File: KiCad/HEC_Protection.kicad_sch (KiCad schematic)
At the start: 32 parts, among them U11 74LS00, U11 74LS32, U12 74LS04, U16 74LS32, U17 74LS74, U18 74LS138, U18 74LS74, U19 74LS30, U22 74LS02, U23 74LS74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

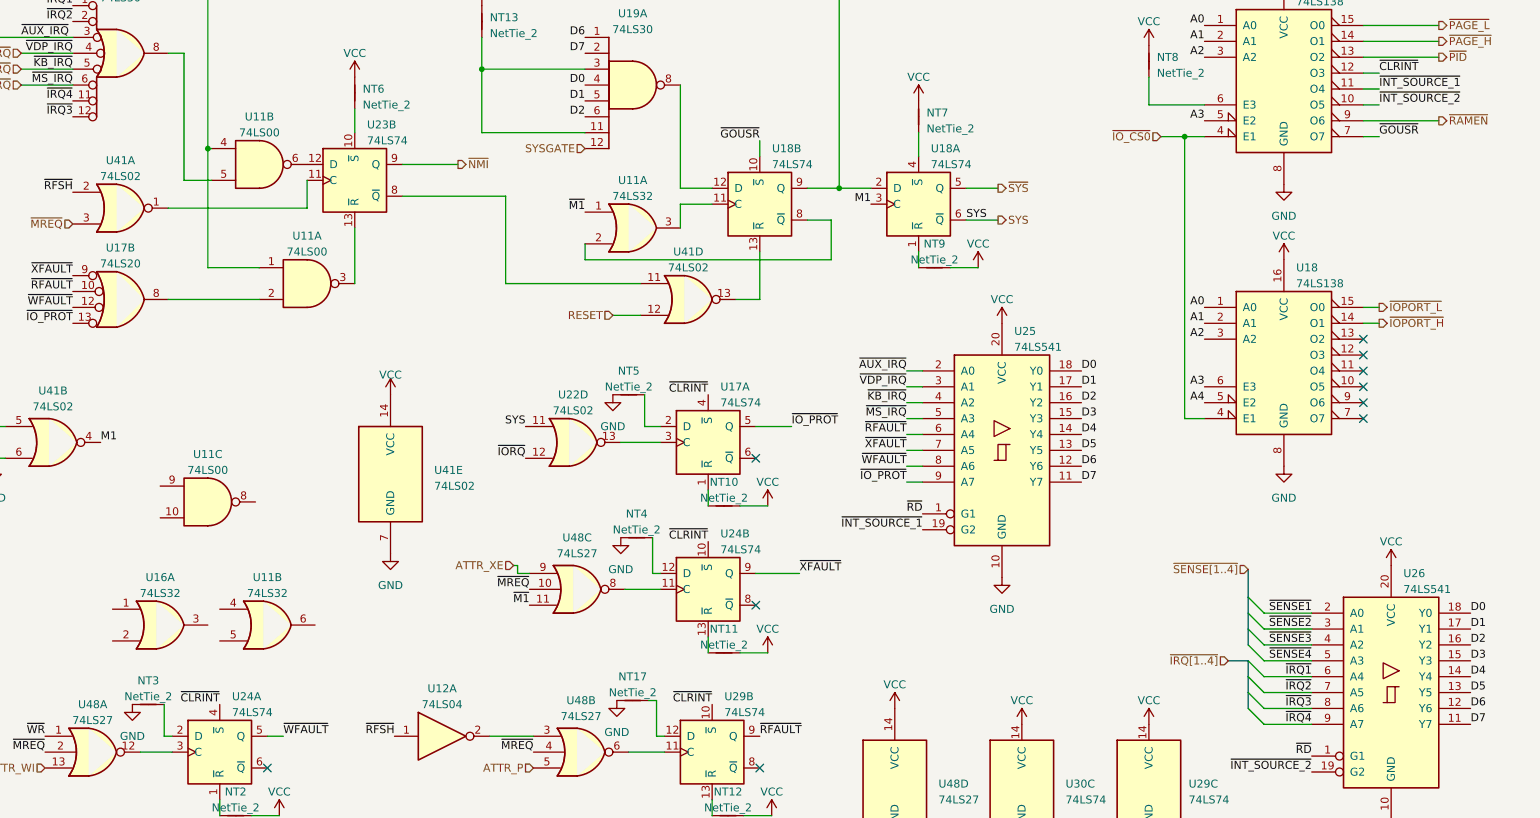
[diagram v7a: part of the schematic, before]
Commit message: Add flash circuit
Changed EEPROM to NOR flash to increase speed. Added circuit to update firmware without requiring a programmer.
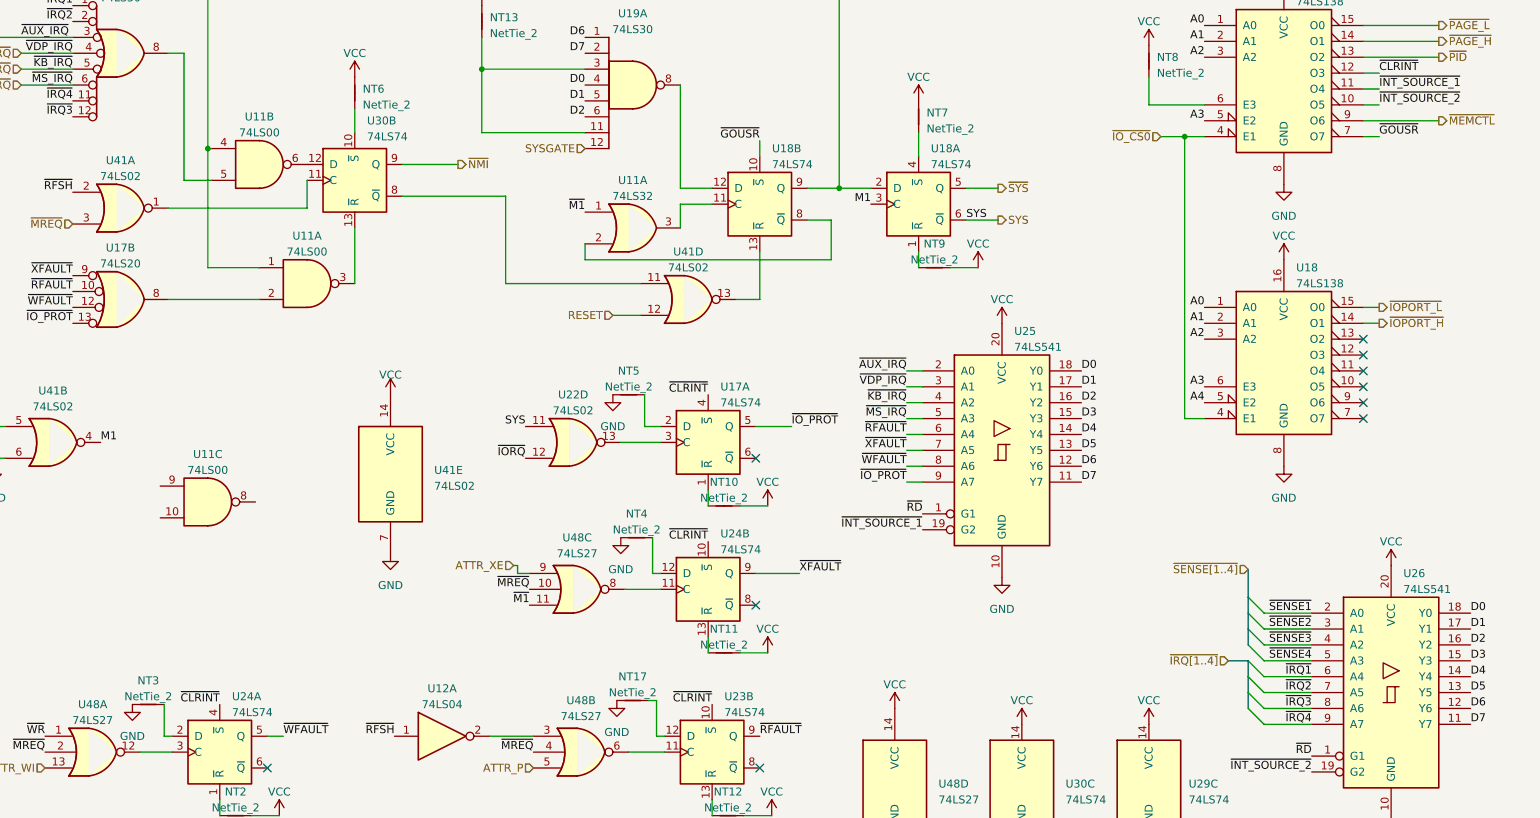
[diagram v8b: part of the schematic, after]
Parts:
- removed U11, U16: 74LS32, Library:DIP-14_W7.62mm_Socket_ThinPads, symbol 74xx:74LS32
- removed unit 2 of U29
- added unit 2 of U30
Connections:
- net ~{CLRINT}: now also U23.10 (~{S})
- net ~{NMI}: now also U30.9 (Q); no longer U23.9 (Q)
- net ~{RFAULT}: now also U23.9 (Q)
- net at U48.6: now also U23.11 (C)
- net at NT17.2: now also U23.12 (D)
- net at NT12.1: now also U23.13 (~{R})
- net at U41.11: now also U30.8 (~{Q}); no longer U23.8 (~{Q})
- net at NT6.1: now also U30.10 (~{S}); no longer U23.10 (~{S})
- net at U41.1: now also U30.11 (C); no longer U23.11 (C)
- net at U11.6: now also U30.12 (D); no longer U23.12 (D)
- net at U11.3: now also U30.13 (~{R}); no longer U23.13 (~{R})
- net ~{RAMEN} renamed ~{MEMCTL}
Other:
- moved on the sheet: U23B
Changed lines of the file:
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@@
     (effects (font (size 1.27 1.27)) (justify right))
   )
-  (hierarchical_label "~{RAMEN}" (shape output) (at 274.955 42.545 0) (fields_autoplaced)
+  (hierarchical_label "~{MEMCTL}" (shape output) (at 274.955 42.545 0) (fields_autoplaced)
     (effects (font (size 1.27 1.27)) (justify left))
   )
@@
     )
   )
-  (symbol (lib_id "74xx:74LS32") (at 87.63 123.19 0) (unit 2)
-    (in_bom yes) (on_board yes) (dnp no) (fields_autoplaced)
-    (property "Reference" "U11" (at 87.63 115.57 0)
-      (effects (font (size 1.27 1.27)))
-    )
-    (property "Value" "74LS32" (at 87.63 118.11 0)
-      (effects (font (size 1.27 1.27)))
-    )
-    (property "Footprint" "Library:DIP-14_W7.62mm_Socket_ThinPads" (at 87.63 123.19 0)
-      (effects (font (size 1.27 1.27)) hide)
-    )
-    (property "Datasheet" "http://www.ti.com/lit/gpn/sn74LS32" (at 87.63 123.19 0)
-      (effects (font (size 1.27 1.27)) hide)
-    )
-    (pin "1")
-    (pin "2")
-    (pin "3")
-    (pin "4")
-    (pin "5")
-    (pin "6")
-    (pin "10")
-    (pin "8")
-    (pin "9")
-    (pin "11")
-    (pin "12")
-    (pin "13")
-    (pin "14")
-    (pin "7")
-    (instances
-      (project "HEC1"
-        (path "/87935374-b60a-4f41-99da-94b76103dd77/73a0c68b-1e42-4c0d-ae31-b1a96d0648bb"
-          (reference "U11") (unit 2)
-        )
-        (path "/87935374-b60a-4f41-99da-94b76103dd77/2930b625-d6a3-4a7f-9d41-a454efcef99d"
-          (reference "U10") (unit 2)
-        )
-      )
-    )
-  )
   (symbol (lib_id "power:VCC") (at 205.105 74.93 0) (unit 1)
     (in_bom yes) (on_board yes) (dnp no) (fields_autoplaced)
@@
         (path "/87935374-b60a-4f41-99da-94b76103dd77/2930b625-d6a3-4a7f-9d41-a454efcef99d"
           (reference "U41") (unit 5)
-        )
-      )
-    )
-  )
-  (symbol (lib_id "74xx:74LS74") (at 158.75 143.51 0) (unit 2)
-    (in_bom yes) (on_board yes) (dnp no) (fields_autoplaced)
-    (property "Reference" "U29" (at 160.7059 134.62 0)
-      (effects (font (size 1.27 1.27)) (justify left))
-    )
-    (property "Value" "74LS74" (at 160.7059 137.16 0)
-      (effects (font (size 1.27 1.27)) (justify left))
-    )
-    (property "Footprint" "Library:DIP-14_W7.62mm_Socket_ThinPads" (at 158.75 143.51 0)
-      (effects (font (size 1.27 1.27)) hide)
-    )
-    (property "Datasheet" "74xx/74hc_hct74.pdf" (at 158.75 143.51 0)
-      (effects (font (size 1.27 1.27)) hide)
-    )
-    (pin "1")
-    (pin "2")
-    (pin "3")
-    (pin "4")
-    (pin "5")
-    (pin "6")
-    (pin "10")
-    (pin "11")
-    (pin "12")
-    (pin "13")
-    (pin "8")
-    (pin "9")
-    (pin "14")
-    (pin "7")
-    (instances
-      (project "HEC1"
-        (path "/87935374-b60a-4f41-99da-94b76103dd77/2930b625-d6a3-4a7f-9d41-a454efcef99d"
-          (reference "U29") (unit 2)
         )
       )
@@
     )
   )
-  (symbol (lib_id "74xx:74LS74") (at 101.6 52.07 0) (unit 2)
-    (in_bom yes) (on_board yes) (dnp no) (fields_autoplaced)
-    (property "Reference" "U23" (at 103.5559 43.18 0)
-      (effects (font (size 1.27 1.27)) (justify left))
-    )
-    (property "Value" "74LS74" (at 103.5559 45.72 0)
-      (effects (font (size 1.27 1.27)) (justify left))
-    )
-    (property "Footprint" "Library:DIP-14_W7.62mm_Socket_ThinPads" (at 101.6 52.07 0)
-      (effects (font (size 1.27 1.27)) hide)
-    )
-    (property "Datasheet" "74xx/74hc_hct74.pdf" (at 101.6 52.07 0)
+  (symbol (lib_id "74xx:74LS74") (at 158.75 143.51 0) (unit 2)
+    (in_bom yes) (on_board yes) (dnp no) (fields_autoplaced)
+    (property "Reference" "U23" (at 160.7059 134.62 0)
+      (effects (font (size 1.27 1.27)) (justify left))
+    )
+    (property "Value" "74LS74" (at 160.7059 137.16 0)
+      (effects (font (size 1.27 1.27)) (justify left))
+    )
+    (property "Footprint" "Library:DIP-14_W7.62mm_Socket_ThinPads" (at 158.75 143.51 0)
+      (effects (font (size 1.27 1.27)) hide)
+    )
+    (property "Datasheet" "74xx/74hc_hct74.pdf" (at 158.75 143.51 0)
       (effects (font (size 1.27 1.27)) hide)
     )
@@
     )
   )
+  (symbol (lib_id "74xx:74LS74") (at 101.6 52.07 0) (unit 2)
+    (in_bom yes) (on_board yes) (dnp no) (fields_autoplaced)
+    (property "Reference" "U30" (at 103.5559 42.545 0)
+      (effects (font (size 1.27 1.27)) (justify left))
+    )
+    (property "Value" "74LS74" (at 103.5559 45.085 0)
+      (effects (font (size 1.27 1.27)) (justify left))
+    )
+    (property "Footprint" "Library:DIP-14_W7.62mm_Socket_ThinPads" (at 101.6 52.07 0)
+      (effects (font (size 1.27 1.27)) hide)
+    )
+    (property "Datasheet" "74xx/74hc_hct74.pdf" (at 101.6 52.07 0)
+      (effects (font (size 1.27 1.27)) hide)
+    )
+    (pin "1")
+    (pin "2")
+    (pin "3")
+    (pin "4")
+    (pin "5")
+    (pin "6")
+    (pin "10")
+    (pin "11")
+    (pin "12")
+    (pin "13")
+    (pin "8")
+    (pin "9")
+    (pin "14")
+    (pin "7")
+    (instances
+      (project "HEC1"
+        (path "/87935374-b60a-4f41-99da-94b76103dd77/2930b625-d6a3-4a7f-9d41-a454efcef99d"
+          (reference "U30") (unit 2)
+        )
+        (path "/87935374-b60a-4f41-99da-94b76103dd77/8e836f45-562c-4e39-882e-9c8153296a93"
+          (reference "U30") (unit 2)
+        )
+      )
+    )
+  )
   (symbol (lib_id "74xx:74LS04") (at 115.57 140.97 0) (unit 1)
     (in_bom yes) (on_board yes) (dnp no) (fields_autoplaced)
@@
         )
       )
-    )
-  )
-  (symbol (lib_id "74xx:74LS32") (at 70.485 123.19 0) (unit 1)
-    (in_bom yes) (on_board yes) (dnp no) (fields_autoplaced)
-    (property "Reference" "U16" (at 70.485 115.57 0)
-      (effects (font (size 1.27 1.27)))
-    )
-    (property "Value" "74LS32" (at 70.485 118.11 0)
-      (effects (font (size 1.27 1.27)))
-    )
-    (property "Footprint" "Library:DIP-14_W7.62mm_Socket_ThinPads" (at 70.485 123.19 0)
-      (effects (font (size 1.27 1.27)) hide)
-    )
-    (property "Datasheet" "http://www.ti.com/lit/gpn/sn74LS32" (at 70.485 123.19 0)
-      (effects (font (size 1.27 1.27)) hide)
-    )
-    (pin "1")
-    (pin "2")
-    (pin "3")
-    (pin "4")
-    (pin "5")
-    (pin "6")
-    (pin "10")
-    (pin "8")
-    (pin "9")
-    (pin "11")
-    (pin "12")
-    (pin "13")
-    (pin "14")
-    (pin "7")
-    (instances
-      (project "HEC1"
-        (path "/87935374-b60a-4f41-99da-94b76103dd77/933a6f90-eb98-4eb1-8c19-8a76228aece1"
-          (reference "U16") (unit 1)
-        )
-        (path "/87935374-b60a-4f41-99da-94b76103dd77/73a0c68b-1e42-4c0d-ae31-b1a96d0648bb"
-          (reference "U16") (unit 1)
-        )
-        (path "/87935374-b60a-4f41-99da-94b76103dd77/2930b625-d6a3-4a7f-9d41-a454efcef99d"
-          (reference "U16") (unit 1)
-        )
-      )
